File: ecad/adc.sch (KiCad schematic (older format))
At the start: 1 part

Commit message: Mostly complete schematic, about to tape out the PCB.
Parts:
- removed U?: AK5578EN, symbol AK5578EN
- added C29: 100p, Capacitors_SMD:C_0603_HandSoldering, symbol C
- added C30, C31: 120p, Capacitors_SMD:C_0603_HandSoldering, symbol C
- added C42, C43, C44, C45, C46, C47, C48, C50, C51, C52, C53, C55: 0.1u, Capacitors_SMD:C_0603_HandSoldering, symbol C
- added C49, C54: 10n, Capacitors_SMD:C_0603_HandSoldering, symbol C
- added C56: 33p, Capacitors_SMD:C_0603_HandSoldering, symbol C
- added L1, L11, L2, L3, L4, L5, L6, L7, L8, L9: 1k@100M, Inductors_SMD:L_0603_HandSoldering, symbol L_Core_Ferrite_Small
- added L10: 15n, Inductors_SMD:L_0603_HandSoldering, symbol L_Small
- added R28, R29: 1k, Resistors_SMD:R_0603_HandSoldering, symbol R
- added R30, R31: 655, Resistors_SMD:R_0603_HandSoldering, symbol R
- added R32, R33: 18, Resistors_SMD:R_0603_HandSoldering, symbol R
- added R34, R35: 10, Resistors_SMD:R_0603_HandSoldering, symbol R
- added R36: 160k, Resistors_SMD:R_0603_HandSoldering, symbol R
- added U11: CB3-3C-40M0000, feetprints:CTS_CB3_oscillator, symbol CB3-3C
- added U12: NC7SZ08M5, TO_SOT_Packages_SMD:SOT-23-5, symbol NC7SZ08M5
- added U13: AD7760, Housings_QFP:LQFP-64_10x10mm_Pitch0.5mm, symbol AD7760
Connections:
- new net: R36.1, U13.17 (RBIAS)
- new net: C56.1, U13.30 (DECAPB)
- new net: C55.1, U13.8 (DECAPA)
- new net: C49.1, R34.2
- new net: U11.3 (Out), U12.1 (A), U12.2 (B)
- new net +5V: C42.1, C53.1, U11.1 (EN), U11.4 (Vcc), U12.5 (Vcc)
- new net 4.096: R35.2
- new net DB0: U13.61 (DB0)
- new net DB1: U13.60 (DB1)
- new net DB10: U13.50 (DB10)
- new net DB11: U13.49 (DB11)
- new net DB12: U13.48 (DB12)
- new net DB13: U13.47 (DB13)
- new net DB14: U13.46 (DB14)
- new net DB15: U13.45 (DB15)
- new net DB2: U13.59 (DB2)
- new net DB3: U13.57 (DB4)
- new net DB4: U13.58 (DB3)
- new net DB5: U13.56 (DB5)
- new net DB6: U13.55 (DB6)
- new net DB7: U13.54 (DB7)
- new net DB8: U13.52 (DB8)
- new net DB9: U13.51 (DB9)
- new net DVdd: L4.1
- new net GND: C42.2, C43.2, C44.2, C45.2, C46.2, C47.2, C48.2, C49.2, C50.2, C51.2, C52.2, C53.2, C54.2, C55.2, C56.2, R36.2, U11.2 (GND), U12.3 (GND), U13.1 (DGND), U13.11 (AGND4), U13.13 (AGND2), U13.16 (AGND2), U13.18 (AGND2), U13.2 (MCLKGND), U13.23 (AGND3), U13.28 (AGND2), U13.29 (AGND3), U13.31 (AGND3), U13.32 (AGND3), U13.34 (AGND1), U13.35 (DGND), U13.42 (DGND), U13.43 (DGND), U13.5 (AGND2), U13.53 (DGND), U13.62 (DGND), U13.64 (DGND), U13.7 (AGND1), U13.9 (REFGND)
- new net InputN: R29.2
- new net InputP: R28.2
- new net MCLK: U12.4 (Y), U13.3 (MCLK)
- new net Pin10(VRefP): C54.1, R35.1, U13.10 (VREFP)
- new net Pin12(Vbuf): L7.2, R34.1, U13.12 (AVDD4)
- new net Pin14(LHS): C51.1, L10.1, L9.2, U13.14 (AVDD2)
- new net Pin15(Vbias): C44.1, L2.2, U13.15 (AVDD2)
- new net Pin24(VDif1): C45.1, L3.2, U13.24 (AVDD3)
- new net Pin27: L10.2, U13.27 (AVDD2)
- new net Pin33(Vmod2): C47.1, L5.2, U13.33 (AVDD1)
- new net Pin4(RHS): C48.1, L6.2, U13.4 (AVDD2)
- new net Pin41(DVdd): C46.1, L4.2, U13.41 (DVDD)
- new net Pin44(Vdrive1): C50.1, L8.2, U13.44 (VDRIVE)
- new net Pin6(Vmod1): C43.1, L1.2, U13.6 (AVDD1)
- new net Pin63(Vdrive2): C52.1, L11.2, U13.63 (VDRIVE)
- new net VDrive: L11.1, L8.1
- new net VINAN: C29.2, C31.2, R29.1, R31.2, U13.20 (VINAN)
- new net VINAP: C29.1, C30.2, R28.1, R30.2, U13.19 (VINAP)
- new net VINN: R32.1, U13.26 (VINN)
- new net VINP: R33.1, U13.25 (VINP)
- new net VOUTAN: C30.1, R30.1, R33.2, U13.21 (VOUTAN)
- new net VOUTAP: C31.1, R31.1, R32.2, U13.22 (VOUTAP)
- new net Vdd1: L1.1, L5.1
- new net Vdd2: L2.1, L6.1, L9.1
- new net Vdd3: L3.1
- new net Vdd4: L7.1
- new net ~CS: U13.40 (~CS)
- new net ~DRDY: U13.38 (~DRDY)
- new net ~RD: U13.39 (~RD)
- new net ~RESET: U13.37 (~RESET)
- new net ~SYNC: U13.36 (~SYNC)
- no-connect marks 3 -> 0
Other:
- note added: "AVDD1: Modulator supply, 2.5V\nAVDD2: General supply 5V \nAVDD3: Differential opamp, 5V\nAVDD4: Reference Buffer, 5V\nDVDD: 2.5V\nVdrive: 2.5V\nMCLK: 5V high level"
- note added: "Connect at pin 9\n"
- note added: "Connect to AGND3"

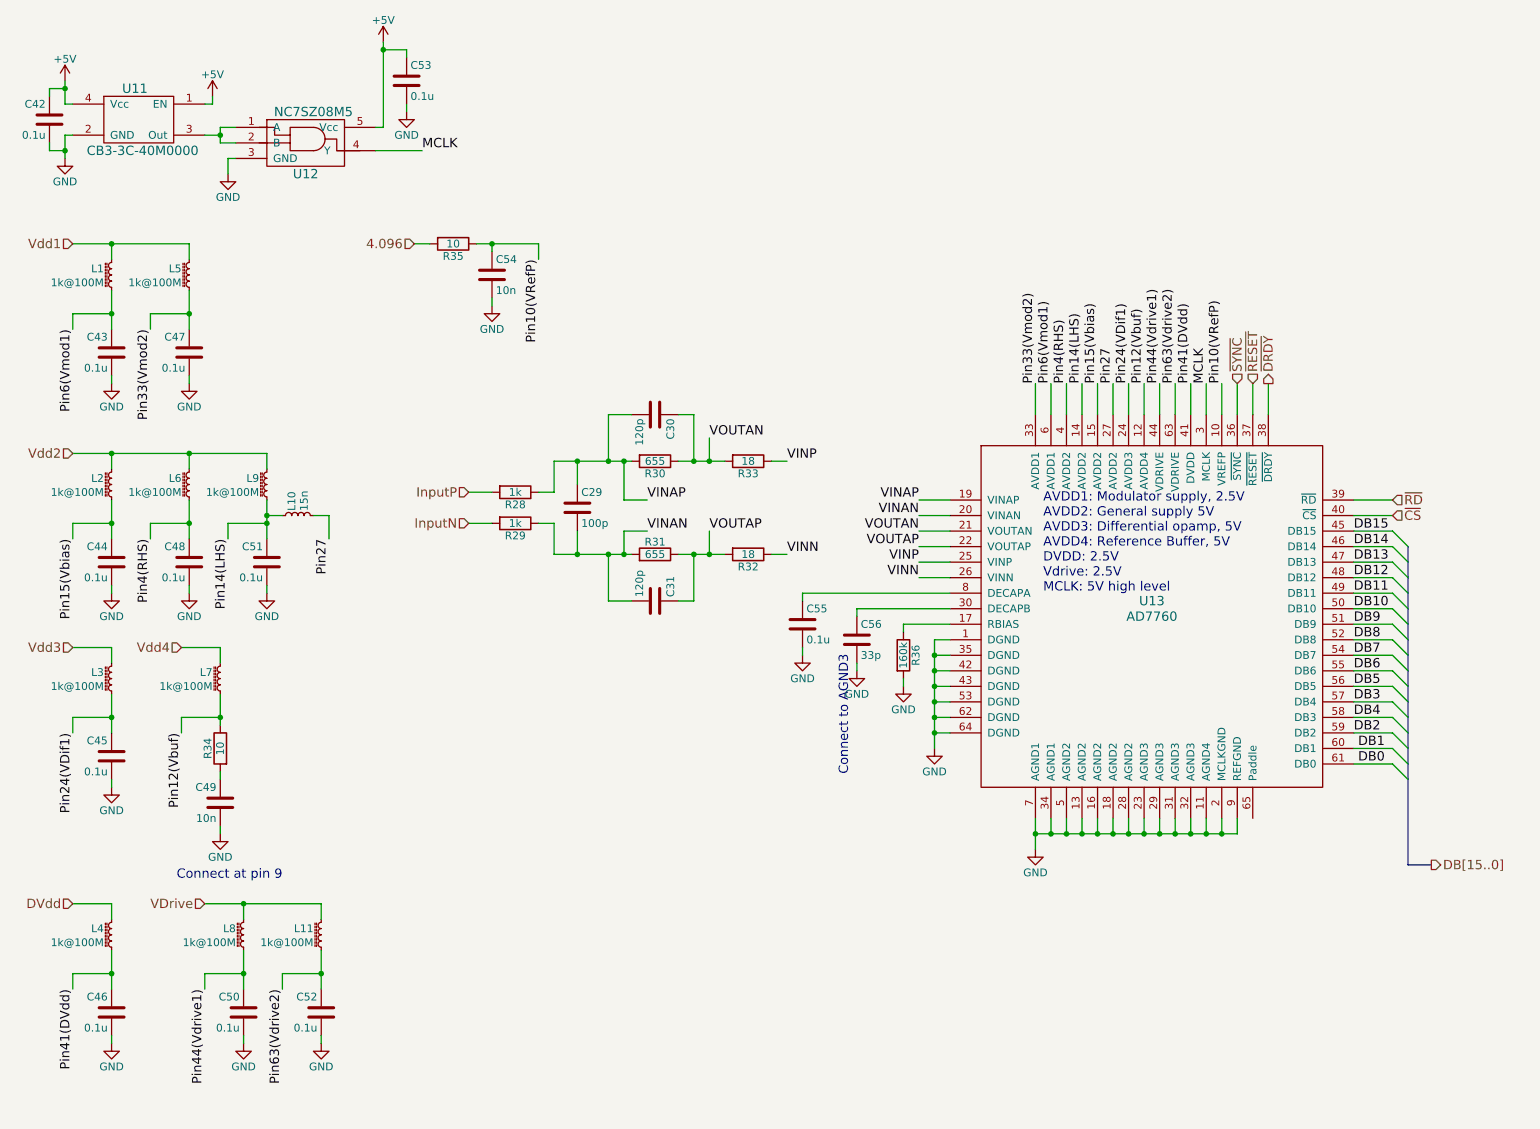
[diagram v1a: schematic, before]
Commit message: First complete pass of PCB with preamp, ADC, and nucleo dev board connections.
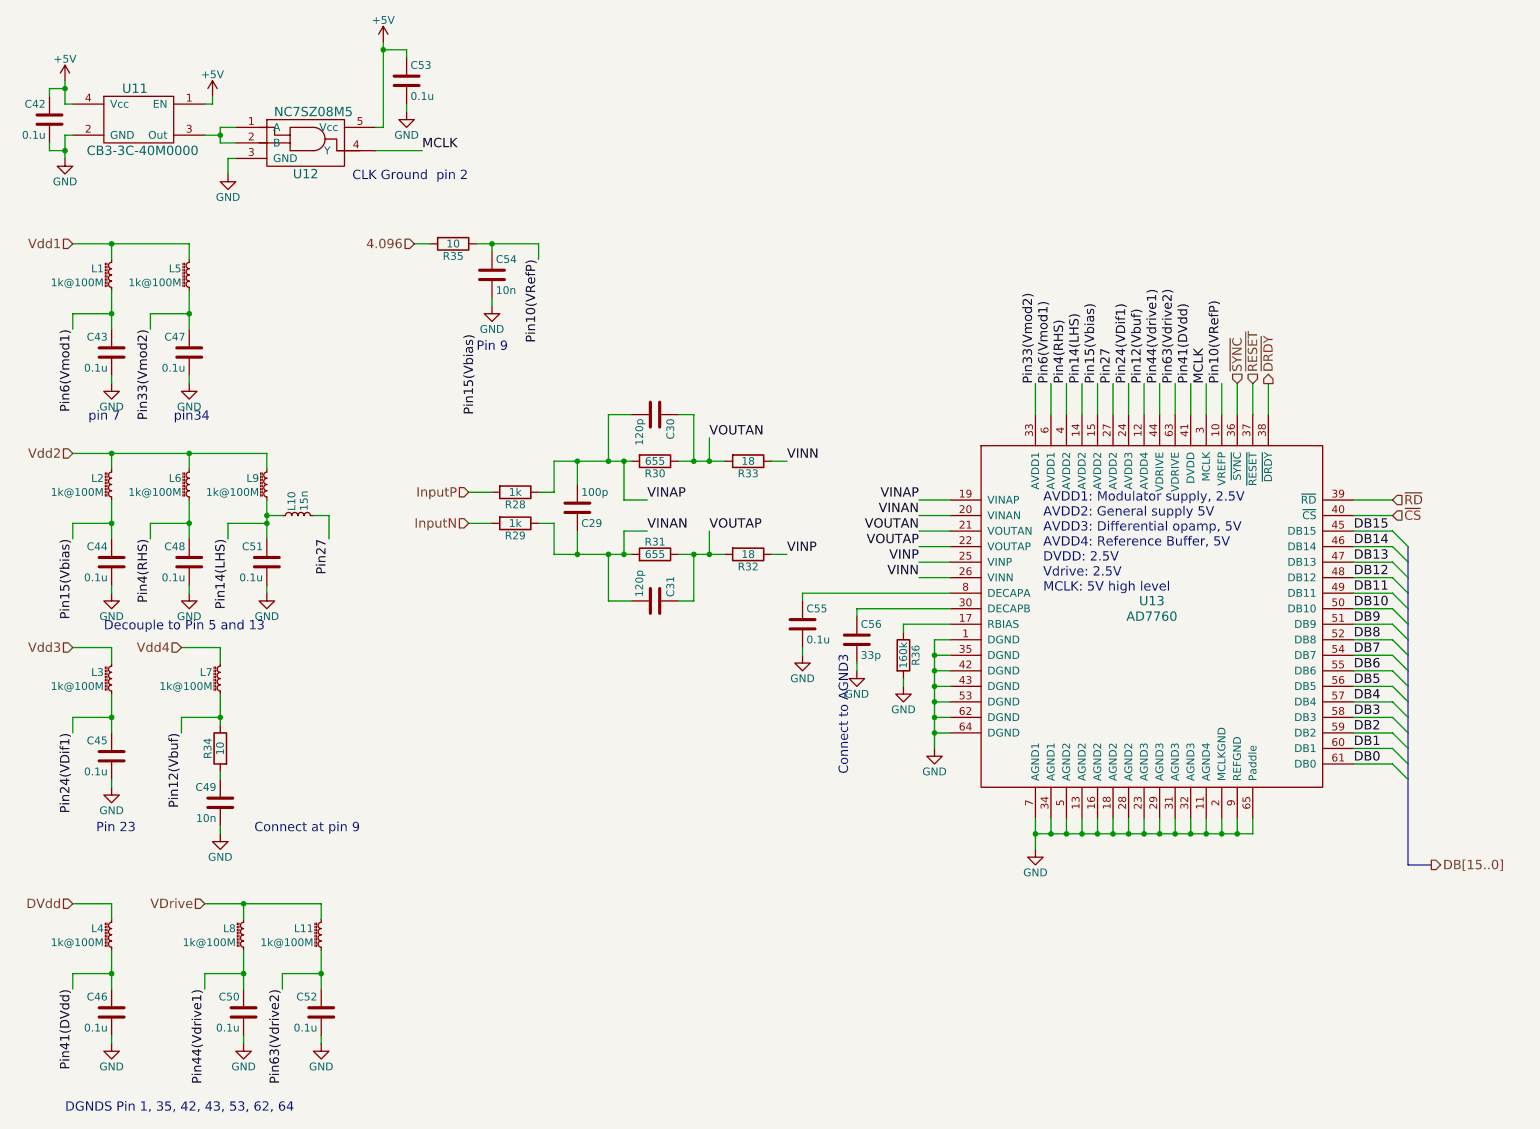
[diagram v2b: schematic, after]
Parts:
- C42, C43, C44, C45, C46, C47, C48, C49, C50, C51, C52, C53, C54, C55, C56: footprint Capacitors_SMD:C_0603_HandSoldering -> Capacitors_SMD:C_0603
- L10: footprint Inductors_SMD:L_0603_HandSoldering -> Inductors_SMD:L_0603
- R34, R35, R36: footprint Resistors_SMD:R_0603_HandSoldering -> Resistors_SMD:R_0603
- U13: footprint Housings_QFP:LQFP-64_10x10mm_Pitch0.5mm -> feetprints:LQFP-EP-64_10x10mm_Pitch0.5mm_6mm_square_paddle
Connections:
- net DB3: now also U13.58 (DB3); no longer U13.57 (DB4)
- net DB4: now also U13.57 (DB4); no longer U13.58 (DB3)
- net GND: now also U13.65 (Paddle)
- net VINAN: now also C29.1; no longer C29.2
- net VINAP: now also C29.2; no longer C29.1
- net VINN: now also R33.1; no longer R32.1
- net VINP: now also R32.1; no longer R33.1
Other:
- note added: "CLK Ground pin 2"
- note added: "DGNDS Pin 1, 35, 42, 43, 53, 62, 64\n"
- note added: "Decouple to Pin 5 and 13\n"
- note added: "Pin 23"
- note added: "Pin 9"
- note added: "pin 7"
- note added: "pin34\n"

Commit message: Source track binary file.
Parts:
- R30, R31: value 655 -> 649
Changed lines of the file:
@@
 P 5350 4100
 F 0 "R31" V 5430 4100 50  0000 C CNN
-F 1 "655" V 5350 4100 50  0000 C CNN
+F 1 "649" V 5350 4100 50  0000 C CNN
 F 2 "Resistors_SMD:R_0603_HandSoldering" V 5280 4100 50  0001 C CNN
 F 3 "" H 5350 4100 50  0001 C CNN
@@
 P 5350 3500
 F 0 "R30" V 5430 3500 50  0000 C CNN
-F 1 "655" V 5350 3500 50  0000 C CNN
+F 1 "649" V 5350 3500 50  0000 C CNN
 F 2 "Resistors_SMD:R_0603_HandSoldering" V 5280 3500 50  0001 C CNN
 F 3 "" H 5350 3500 50  0001 C CNN

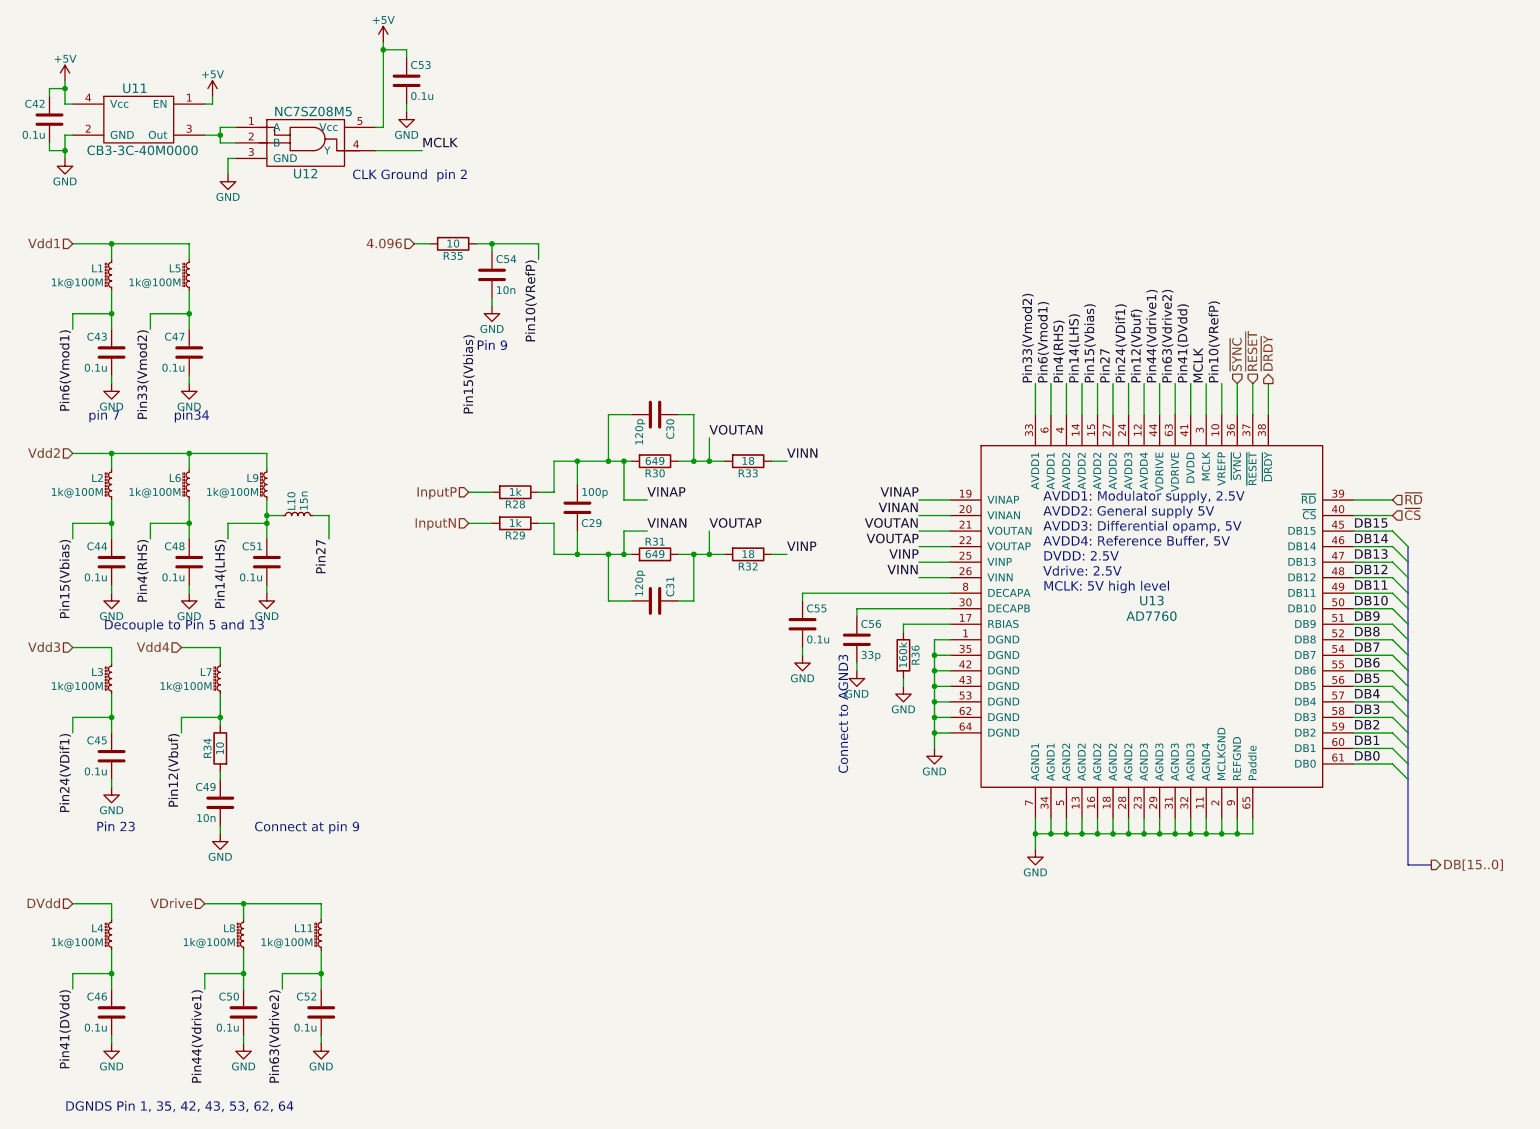
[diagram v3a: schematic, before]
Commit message: Slight changes to simulation and ecad with new changes before rollback to old changes.
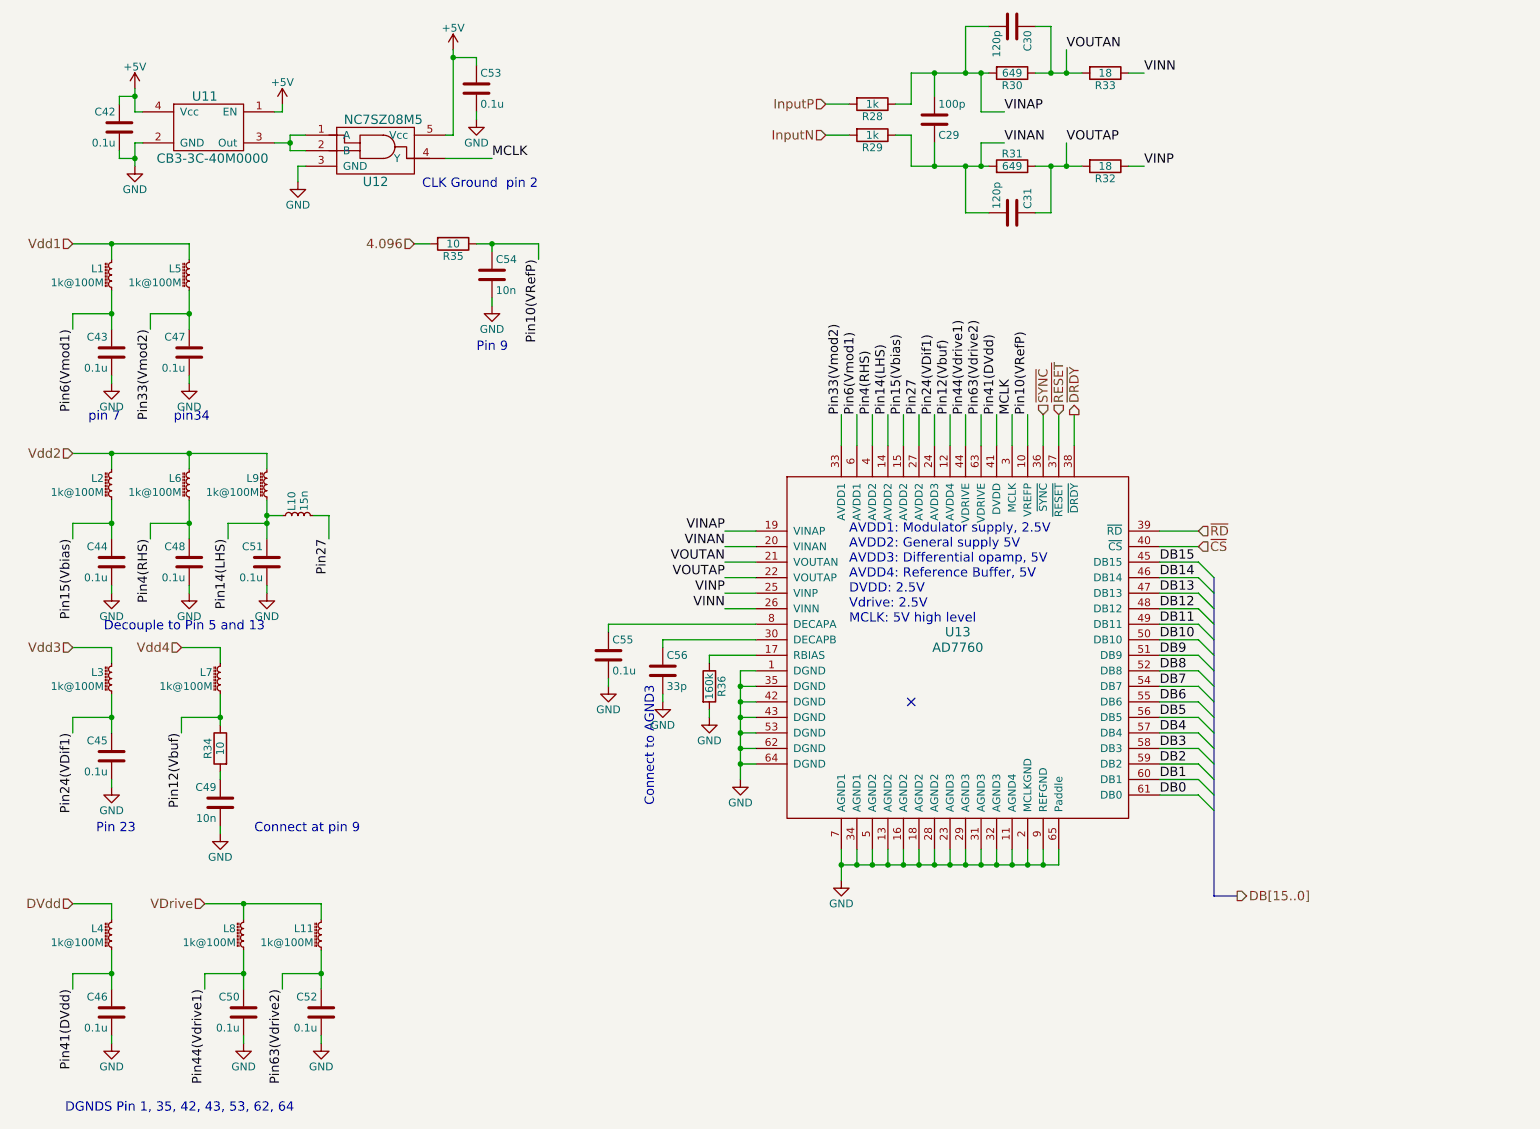
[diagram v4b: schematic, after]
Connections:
- no-connect marks 0 -> 1
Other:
- moved on the sheet: C29, C30, C31, C42, C53, C55, C56, R28, R29, R30, R31, R32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
